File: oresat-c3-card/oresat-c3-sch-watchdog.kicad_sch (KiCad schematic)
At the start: 35 parts, among them U28 TLV1704-SEP

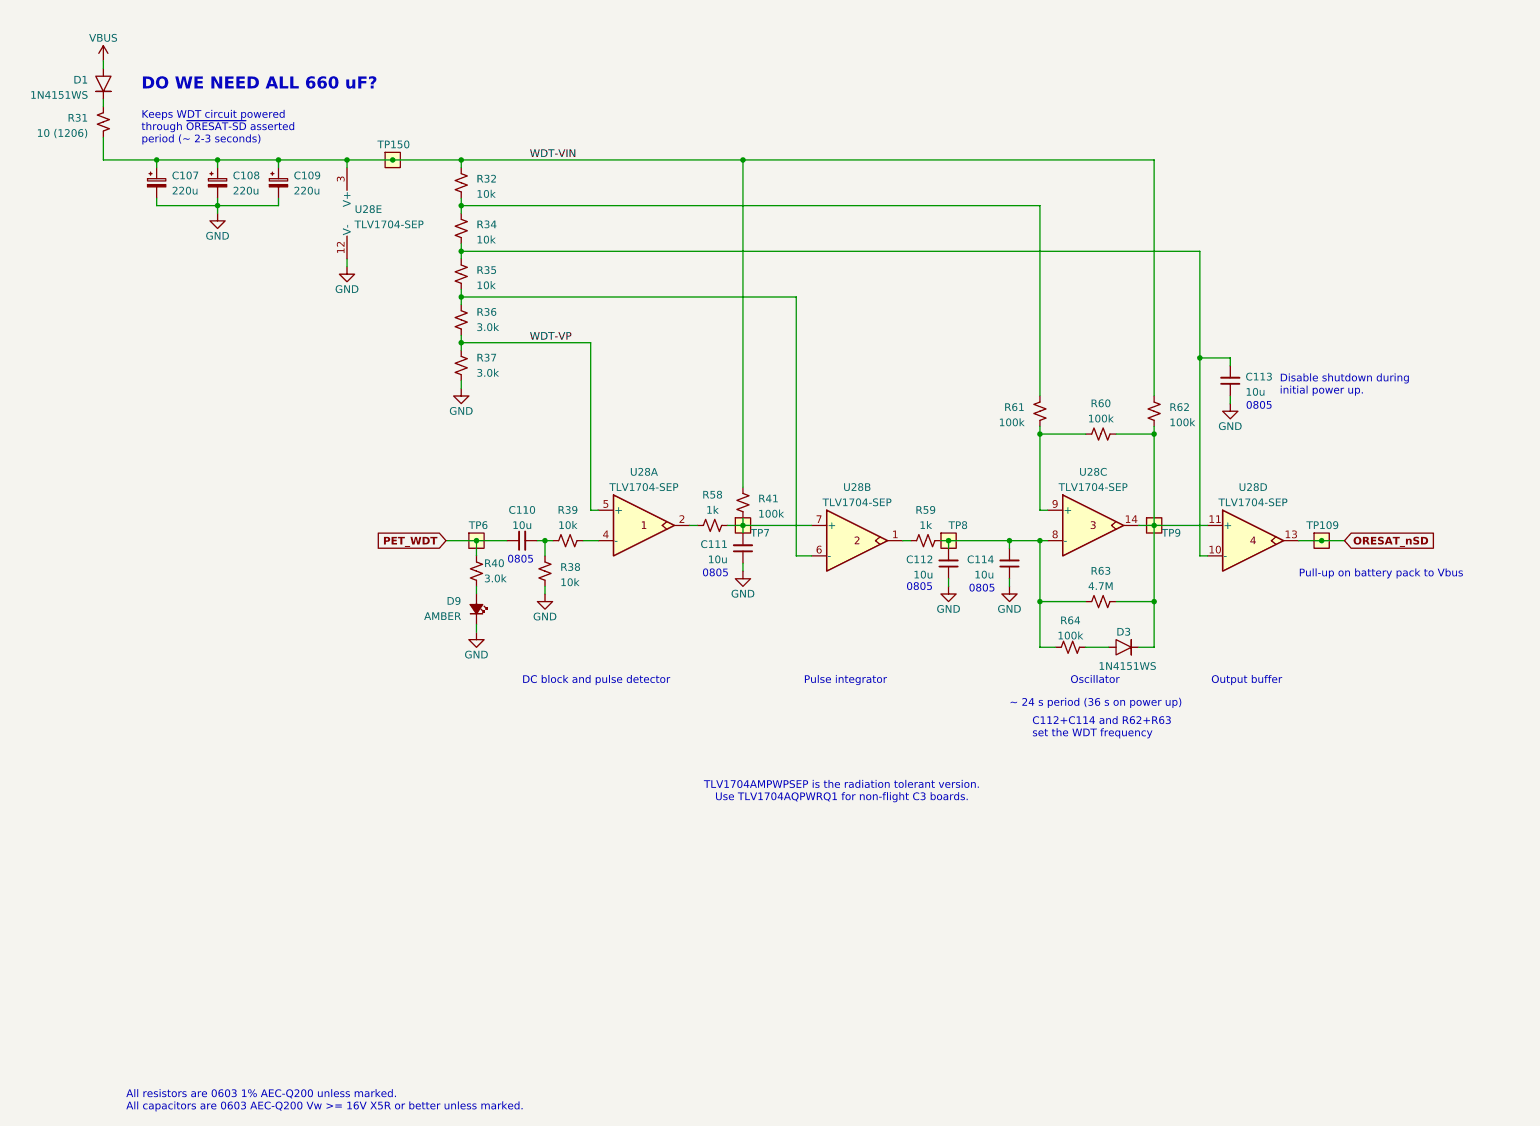
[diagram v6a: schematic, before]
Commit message: Changed WDT tantalums to space-rated tantalums (fun) and fixed some BOM issues. Also possibly more silk screen cleanup.
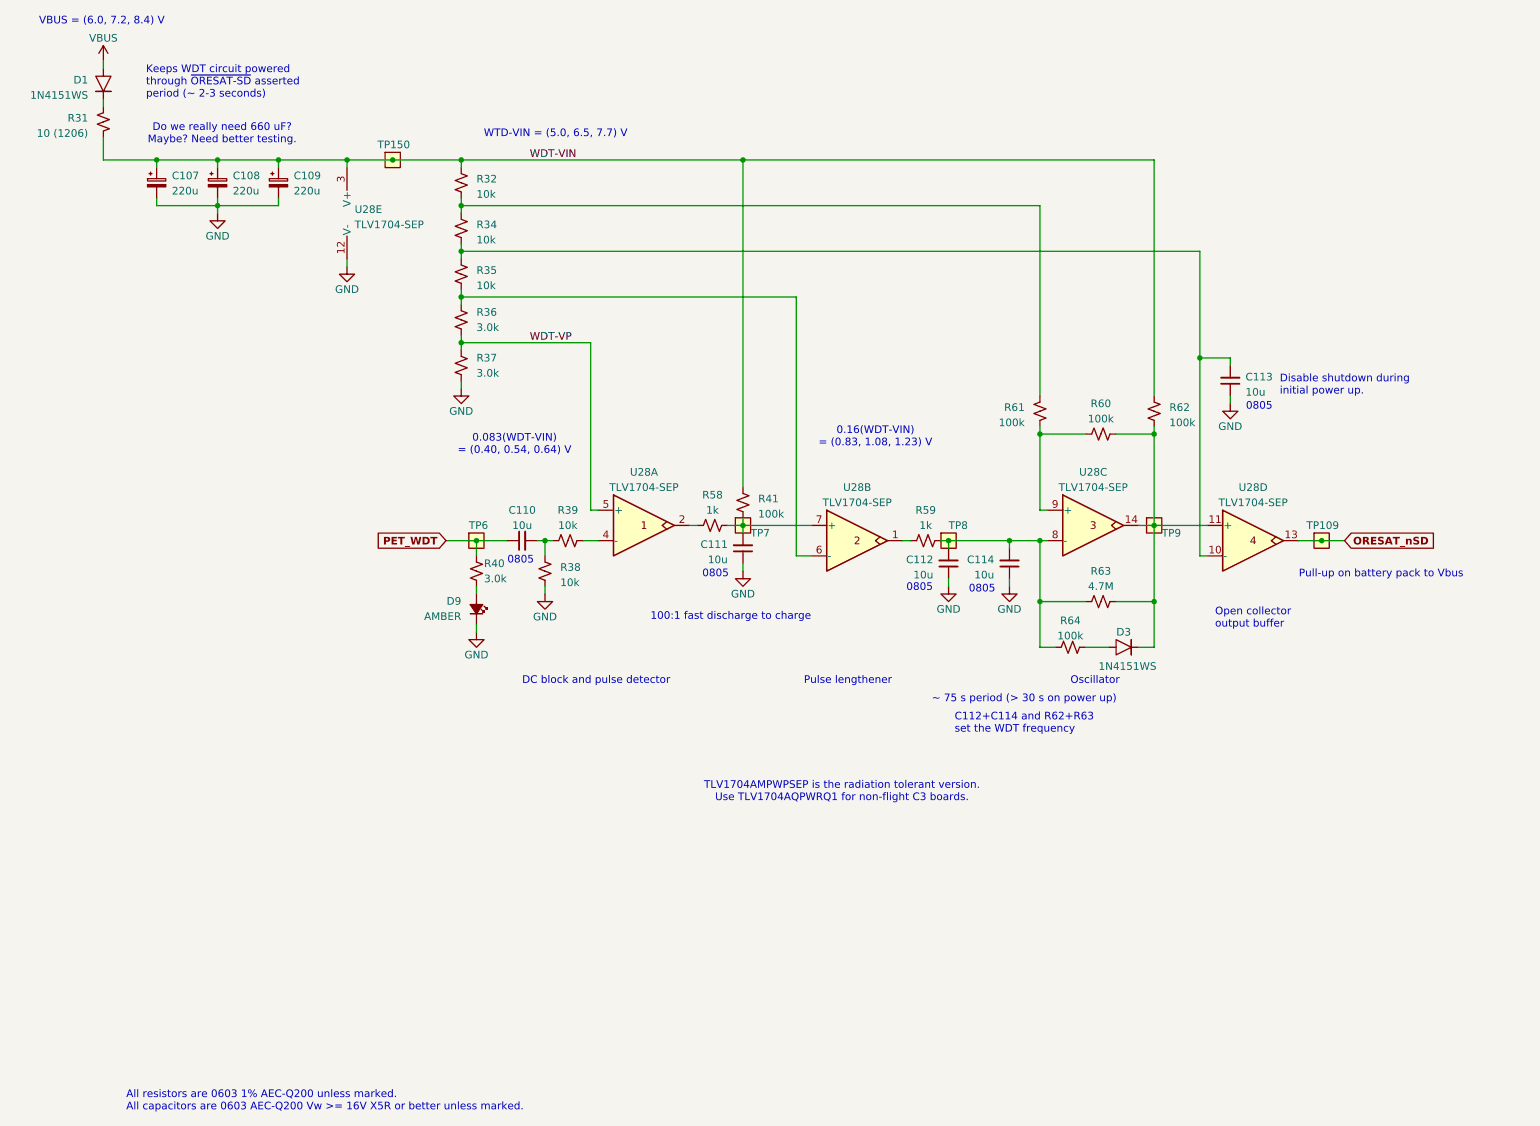
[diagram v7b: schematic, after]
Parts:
- C107, C108, C109: DPN 478-12572-1-ND -> 581-TBJE227K016LBSZ0; DST Digi-Key -> Mouser; MFR AVX Corporation -> KYOCERA AVX; MPN TPSE227K016T0100V -> TBJE227K016LBSZ0000
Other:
- note added: "0.083(WDT-VIN) = (0.40, 0.54, 0.64) V"
- note added: "0.16(WDT-VIN) = (0.83, 1.08, 1.23) V"
- note added: "100:1 fast discharge to charge"
- note added: "Do we really need 660 uF? Maybe? Need better testing."
- note added: "Open collector output buffer"
- note added: "Pulse lengthener"
- note added: "VBUS = (6.0, 7.2, 8.4) V"
- note added: "WTD-VIN = (5.0, 6.5, 7.7) V"
- note added: "~ 75 s period (> 30 s on power up)"
- note removed: "DO WE NEED ALL 660 uF?"
- note removed: "Output buffer"
- note removed: "Pulse integrator"
- note removed: "~ 24 s period (36 s on power up)"
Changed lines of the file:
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@@
 		(company "Portland State Aerospace Society")
 	)
+	(text "100:1 fast discharge to charge"
+		(exclude_from_sim no)
+		(at 220.218 177.8 0)
+		(effects
+			(font
+				(size 1.27 1.27)
+			)
+		)
+	)
 	(text "0805"
 		(exclude_from_sim no)
@@
 		)
 	)
-	(text "Pulse integrator"
+	(text "VBUS = (6.0, 7.2, 8.4) V"
+		(exclude_from_sim no)
+		(at 115.316 78.486 0)
+		(effects
+			(font
+				(size 1.27 1.27)
+			)
+		)
+	)
+	(text "Pulse lengthener"
 		(exclude_from_sim no)
 		(at 232.41 189.23 0)
@@
 	(text "C112+C114 and R62+R63 \nset the WDT frequency"
 		(exclude_from_sim no)
-		(at 270.51 198.12 0)
+		(at 257.556 197.358 0)
 		(effects
 			(font
@@
 		)
 	)
+	(text "Do we really need 660 uF? \nMaybe? Need better testing."
+		(exclude_from_sim no)
+		(at 135.382 97.282 0)
+		(effects
+			(font
+				(size 1.27 1.27)
+			)
+		)
+	)
 	(text "0805"
 		(exclude_from_sim no)
@@
 		)
 	)
+	(text "WTD-VIN = (5.0, 6.5, 7.7) V"
+		(exclude_from_sim no)
+		(at 191.008 97.282 0)
+		(effects
+			(font
+				(size 1.27 1.27)
+			)
+		)
+	)
 	(text "DC block and pulse detector"
 		(exclude_from_sim no)
@@
 		)
 	)
-	(text "Output buffer"
+	(text "Open collector\noutput buffer"
 		(exclude_from_sim no)
-		(at 300.355 189.23 0)
+		(at 300.99 179.832 0)
 		(effects
 			(font
@@
 		)
 	)
-	(text "DO WE NEED ALL 660 uF?"
+	(text "0805"
 		(exclude_from_sim no)
-		(at 121.92 90.17 0)
+		(at 262.128 173.228 0)
 		(effects
 			(font
-				(size 2 2)
-				(thickness 0.4)
-				(bold yes)
-				(color 255 0 0 1)
+				(size 1.27 1.27)
 			)
-			(justify left bottom)
 		)
 	)
-	(text "0805"
+	(text "0.16(WDT-VIN) \n= (0.83, 1.08, 1.23) V"
 		(exclude_from_sim no)
-		(at 262.128 173.228 0)
+		(at 244.348 147.828 0)
 		(effects
 			(font
@@
 	(text "Keeps WDT circuit powered\nthrough ~{ORESAT-SD} asserted\nperiod (~ 2-3 seconds)"
 		(exclude_from_sim no)
-		(at 121.92 99.06 0)
+		(at 122.682 91.44 0)
 		(effects
 			(font
@@
 		)
 	)
-	(text "~ 24 s period (36 s on power up)"
+	(text "~ 75 s period (> 30 s on power up)"
 		(exclude_from_sim no)
-		(at 266.7 193.04 0)
+		(at 253.746 192.278 0)
 		(effects
 			(font
@@
 		)
 	)
+	(text "0.083(WDT-VIN) \n= (0.40, 0.54, 0.64) V"
+		(exclude_from_sim no)
+		(at 184.15 149.098 0)
+		(effects
+			(font
+				(size 1.27 1.27)
+			)
+		)
+	)
 	(junction
 		(at 134.62 109.22)
@@
 			)
 		)
-		(property "Datasheet" "~"
+		(property "Datasheet" "https://www.mouser.com/catalog/specsheets/KYOCERA_FINAL%20Catalog%20Datasheet.pdf"
 			(at 144.78 105.41 0)
 			(effects
@@
 			)
 		)
-		(property "Description" "220µF Molded Tantalum Capacitors 16V 2917 (7343 Metric) 100mOhm @ 100kHz"
+		(property "Description" "220µF Molded Tantalum Capacitors 16V 2917 (7343 Metric) - SPECIAL"
 			(at 144.78 105.41 0)
 			(effects
@@
 			)
 		)
-		(property "DPN" "478-12572-1-ND"
+		(property "DPN" "581-TBJE227K016LBSZ0"
 			(at 144.78 105.41 0)
 			(effects
@@
 			)
 		)
-		(property "DST" "Digi-Key"
+		(property "DST" "Mouser"
 			(at 144.78 105.41 0)
 			(effects
@@
 			)
 		)
-		(property "MFR" "AVX Corporation"
+		(property "MFR" "KYOCERA AVX"
 			(at 144.78 105.41 0)
 			(effects
@@
 			)
 		)
-		(property "MPN" "TPSE227K016T0100V"
+		(property "MPN" "TBJE227K016LBSZ0000"
 			(at 144.78 105.41 0)
 			(effects
@@
 			)
 		)
-		(property "Datasheet" "~"
+		(property "Datasheet" "https://www.mouser.com/catalog/specsheets/KYOCERA_FINAL%20Catalog%20Datasheet.pdf"
 			(at 124.46 105.41 0)
 			(effects
@@
 			)
 		)
-		(property "Description" "220µF Molded Tantalum Capacitors 16V 2917 (7343 Metric) 100mOhm @ 100kHz"
+		(property "Description" "220µF Molded Tantalum Capacitors 16V 2917 (7343 Metric) - SPECIAL"
 			(at 124.46 105.41 0)
 			(effects
@@
 			)
 		)
-		(property "DPN" "478-12572-1-ND"
+		(property "DPN" "581-TBJE227K016LBSZ0"
 			(at 124.46 105.41 0)
 			(effects
@@
 			)
 		)
-		(property "DST" "Digi-Key"
+		(property "DST" "Mouser"
 			(at 124.46 105.41 0)
 			(effects
@@
 			)
 		)
-		(property "MFR" "AVX Corporation"
+		(property "MFR" "KYOCERA AVX"
 			(at 124.46 105.41 0)
 			(effects
@@
 			)
 		)
-		(property "MPN" "TPSE227K016T0100V"
+		(property "MPN" "TBJE227K016LBSZ0000"
 			(at 124.46 105.41 0)
 			(effects
@@
 			)
 		)
-		(property "Datasheet" "~"
+		(property "Datasheet" "https://www.mouser.com/catalog/specsheets/KYOCERA_FINAL%20Catalog%20Datasheet.pdf"
 			(at 134.62 105.41 0)
 			(effects
@@
 			)
 		)
-		(property "Description" "220µF Molded Tantalum Capacitors 16V 2917 (7343 Metric) 100mOhm @ 100kHz"
+		(property "Description" "220µF Molded Tantalum Capacitors 16V 2917 (7343 Metric) - SPECIAL"
 			(at 134.62 105.41 0)
 			(effects
@@
 			)
 		)
-		(property "DPN" "478-12572-1-ND"
+		(property "DPN" "581-TBJE227K016LBSZ0"
 			(at 134.62 105.41 0)
 			(effects
@@
 			)
 		)
-		(property "DST" "Digi-Key"
+		(property "DST" "Mouser"
 			(at 134.62 105.41 0)
 			(effects
@@
 			)
 		)
-		(property "MFR" "AVX Corporation"
+		(property "MFR" "KYOCERA AVX"
 			(at 134.62 105.41 0)
 			(effects
@@
 			)
 		)
-		(property "MPN" "TPSE227K016T0100V"
+		(property "MPN" "TBJE227K016LBSZ0000"
 			(at 134.62 105.41 0)
 			(effects
